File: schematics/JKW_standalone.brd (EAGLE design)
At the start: 159.4 x 80.7 mm, 251 parts, among them IC1 4093D, IC2 LM1458D, IC4 ATMEGA2560-16AU, Q1 BSS84, Q10 BSS84, Q11 BSS84, Q2 BSS84, Q3 BSS84, Q4 BSS84, Q5 BSS84, Q6 BSS84, Q7 BSS84, Q8 BSS84, Q9 BSS84, T1 Mouser: 771-2N7002BK215 , N-C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, T10 Mouser: 771-2N7002BK215 , N-C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, T11 Mouser: 771-2N7002BK215 , N-C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, T12 Mouser: 771-2N7002BK215 , N-C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, T13 Mouser: 771-2N7002BK215 , N-C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, T2 Mouser: 771-2N7002BK215 , N-C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, T3 Mouser: 771-2N7002BK215 , N-C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, T5 Mouser: 771-2N7002BK215 , N-C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, T6 Mouser: 771-2N7002BK215 , N-C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, T7 Mouser: 771-2N7002BK215 , N-C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, T8 Mouser: 771-2N7002BK215 , N-C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, T9 Mouser: 771-2N7002BK215 , N-C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, U4 MCP2515, U5 MCP2551

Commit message: Board equiped with low passes
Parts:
- added C15, C16, C20, C5, C7: 100nF, RCLDT:0805
- R_E2_3, R_E2_4: value n.b. / 0R -> 0R / n.b.
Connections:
- net BL_L_IN: now also C5.1
- net BL_R_IN: now also C7.1
- net GND: now also C15.2, C16.1, C20.1, C5.2, C7.2
- net HB_IN: now also C15.1
- net NG_IN: now also C20.2
- net OIL_PR_IN: now also C16.2
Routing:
- net NG_IN: track 47.9 -> 49.6 mm
- net BL_R_IN: track 19.2 -> 20.4 mm
- net BL_L_IN: track 50.9 -> 52.0 mm
- net OIL_PR_IN: track 66.6 -> 67.3 mm
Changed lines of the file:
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@@
 <?xml version="1.0" encoding="utf-8"?>
 <!DOCTYPE eagle SYSTEM "eagle.dtd">
-<eagle version="6.4">
+<eagle version="6.2">
 <drawing>
 <settings>
@@
 <layer number="27" name="tValues" color="7" fill="1" visible="yes" active="yes"/>
 <layer number="28" name="bValues" color="7" fill="1" visible="yes" active="yes"/>
-<layer number="29" name="tStop" color="7" fill="3" visible="no" active="yes"/>
-<layer number="30" name="bStop" color="7" fill="6" visible="no" active="yes"/>
+<layer number="29" name="tStop" color="7" fill="3" visible="yes" active="yes"/>
+<layer number="30" name="bStop" color="7" fill="6" visible="yes" active="yes"/>
 <layer number="31" name="tCream" color="7" fill="4" visible="yes" active="yes"/>
 <layer number="32" name="bCream" color="7" fill="5" visible="yes" active="yes"/>
@@
 <text x="150" y="20.5" size="1.778" layer="1" font="vector" ratio="20">TOP</text>
 <text x="154.5" y="20.5" size="1.778" layer="16" font="vector" ratio="20" rot="MR0">BOT</text>
-<circle x="5.4" y="16.7" radius="2.5" width="0.4064" layer="39"/>
+<circle x="5.4" y="16.7" radius="3.5" width="0.4064" layer="39"/>
 <circle x="5.9" y="61.8" radius="2.5" width="0.4064" layer="39"/>
 <text x="101.3" y="19.1" size="1.778" layer="16" font="vector" ratio="13" rot="MR0">1</text>
@@
 </class>
 </classes>
-<designrules name="default">
+<designrules>
 <description language="de">DRC von Lutz
 Via´s bis 0.6mm mit Lötstoplack überzogen
@@
 <element name="U4" library="microchip_can" package="SO-18W" value="MCP2515" x="24.3" y="49.9"/>
 <element name="U5" library="skpang_lib" package="SO-08M" value="MCP2551" x="15.5" y="40.2" rot="R180"/>
-<element name="R_E2_3" library="RCLDT" package="0805" value="n.b. / 0R" x="11.7" y="12.4" rot="MR90"/>
-<element name="R_E2_4" library="RCLDT" package="0805" value="n.b. / 0R" x="17.2" y="12.4" rot="MR270"/>
+<element name="R_E2_3" library="RCLDT" package="0805" value="0R / n.b. " x="11.7" y="12.4" rot="MR90"/>
+<element name="R_E2_4" library="RCLDT" package="0805" value="0R / n.b. " x="17.2" y="12.4" rot="MR270"/>
 <element name="R13" library="RCLDT" package="0805" value="4.7k" x="18" y="33.7" rot="R90"/>
 <element name="R10" library="RCLDT" package="0805" value="100" x="10.8" y="37.2"/>
@@
 </element>
 <element name="RX1" library="pinhead" package="1X02" value="" x="61.9" y="8.4" rot="R90"/>
+<element name="C5" library="RCLDT" package="0805" value="100nF" x="11.8" y="21.5"/>
+<element name="C7" library="RCLDT" package="0805" value="100nF" x="34.7" y="34.3" rot="MR0"/>
+<element name="C15" library="RCLDT" package="0805" value="100nF" x="35.3" y="10" rot="MR270"/>
+<element name="C16" library="RCLDT" package="0805" value="100nF" x="41.8" y="14.6" rot="MR270"/>
+<element name="C20" library="RCLDT" package="0805" value="100nF" x="42.4" y="13.4"/>
 </elements>
 <signals>
@@
 <contactref element="U4" pad="9"/>
 <wire x1="22.25" y1="36.1" x2="22" y2="36.1" width="0.254" layer="1"/>
-<via x="33.25" y="35.375" extent="1-16" drill="0.3"/>
+<via x="34.85" y="35.775" extent="1-16" drill="0.3"/>
 <contactref element="R13" pad="1"/>
 <contactref element="C22" pad="1"/>
@@
 <via x="46.25" y="56.15" extent="1-16" drill="0.3"/>
 <via x="34.35" y="48.95" extent="1-16" drill="0.3"/>
+<contactref element="C5" pad="2"/>
+<contactref element="C7" pad="2"/>
+<contactref element="C15" pad="2"/>
+<contactref element="C16" pad="1"/>
+<contactref element="C20" pad="1"/>
 </signal>
 <signal name="DZ">
@@
 <wire x1="42.6" y1="10.8" x2="42.6" y2="12" width="0.254" layer="1"/>
 <via x="42.6" y="12" extent="1-16" drill="0.3"/>
+<contactref element="C20" pad="2"/>
+<wire x1="43.416" y1="13.4" x2="43.416" y2="12.816" width="0.254" layer="1"/>
+<wire x1="43.416" y1="12.816" x2="42.6" y2="12" width="0.254" layer="1"/>
 </signal>
 <signal name="D42">
@@
 <wire x1="8.9" y1="24.9" x2="8.9" y2="22.6" width="0.254" layer="1"/>
 <wire x1="8.9" y1="22.6" x2="7.1" y2="22.6" width="0.254" layer="1"/>
-<wire x1="10.1" y1="19.116" x2="8.9" y2="20.316" width="0.254" layer="1"/>
-<wire x1="8.9" y1="20.316" x2="8.9" y2="22.6" width="0.254" layer="1"/>
+<contactref element="C5" pad="1"/>
+<wire x1="10.1" y1="19.116" x2="10.1" y2="19.932" width="0.254" layer="1"/>
+<wire x1="10.784" y1="20.616" x2="10.784" y2="21.5" width="0.254" layer="1"/>
+<wire x1="10.784" y1="20.616" x2="10.1" y2="19.932" width="0.254" layer="1"/>
+<wire x1="10.784" y1="21.5" x2="10" y2="21.5" width="0.254" layer="1"/>
+<wire x1="10" y1="21.5" x2="8.9" y2="22.6" width="0.254" layer="1"/>
 </signal>
 <signal name="HB_IN">
@@
 <wire x1="23.2" y1="38.316" x2="23.3" y2="38.416" width="0.254" layer="1"/>
 <wire x1="23.3" y1="38.416" x2="26.2" y2="38.416" width="0.254" layer="1"/>
+<contactref element="C15" pad="1"/>
+<wire x1="35.3" y1="11.016" x2="35.316" y2="11.016" width="0.254" layer="16"/>
+<wire x1="35.316" y1="11.016" x2="35.5" y2="11.2" width="0.254" layer="16"/>
 </signal>
 <signal name="BL_R_IN">
@@
 <wire x1="36.94" y1="34.36" x2="36.8" y2="34.5" width="0.254" layer="16"/>
 <via x="36.8" y="34.5" extent="1-16" drill="0.3"/>
-<wire x1="36.8" y1="34.5" x2="28.2" y2="34.5" width="0.254" layer="1"/>
 <via x="26.4" y="34.5" extent="1-16" drill="0.3"/>
+<wire x1="36.8" y1="34.5" x2="28.2" y2="34.5" width="0.254" layer="1"/>
 <wire x1="28.2" y1="34.5" x2="26.4" y2="34.5" width="0.254" layer="1"/>
 <wire x1="28.216" y1="34.484" x2="28.2" y2="34.5" width="0.254" layer="1"/>
@@
 <wire x1="28.3" y1="34.984" x2="28.3" y2="34.6" width="0.254" layer="1"/>
 <wire x1="28.3" y1="34.6" x2="28.2" y2="34.5" width="0.254" layer="1"/>
+<contactref element="C7" pad="1"/>
+<wire x1="35.716" y1="34.3" x2="36.6" y2="34.3" width="0.254" layer="16"/>
+<wire x1="36.6" y1="34.3" x2="36.8" y2="34.5" width="0.254" layer="16"/>
 </signal>
 <signal name="BL_R_IN_H">
@@
 <wire x1="49.8" y1="12.9" x2="50.4" y2="13.5" width="0.254" layer="16"/>
 <contactref element="R_HB1" pad="2"/>
-<wire x1="49.8" y1="12.9" x2="36.1" y2="12.9" width="0.254" layer="16"/>
+<wire x1="49.8" y1="12.9" x2="41.9" y2="12.9" width="0.254" layer="16"/>
+<wire x1="41.9" y1="12.9" x2="36.1" y2="12.9" width="0.254" layer="16"/>
 <wire x1="36.1" y1="12.9" x2="35.4" y2="13.6" width="0.254" layer="16"/>
 <wire x1="35.4" y1="13.6" x2="35.4" y2="31.4" width="0.254" layer="16"/>
@@
 <via x="21.5" y="33.2" extent="1-16" drill="0.3"/>
 <wire x1="21.5" y1="33.2" x2="21.5" y2="32.016" width="0.254" layer="16"/>
+<contactref element="C16" pad="2"/>
+<wire x1="41.8" y1="13.584" x2="41.8" y2="13" width="0.254" layer="16"/>
+<wire x1="41.8" y1="13" x2="41.9" y2="12.9" width="0.254" layer="16"/>
 </signal>
 <signal name="N$2">

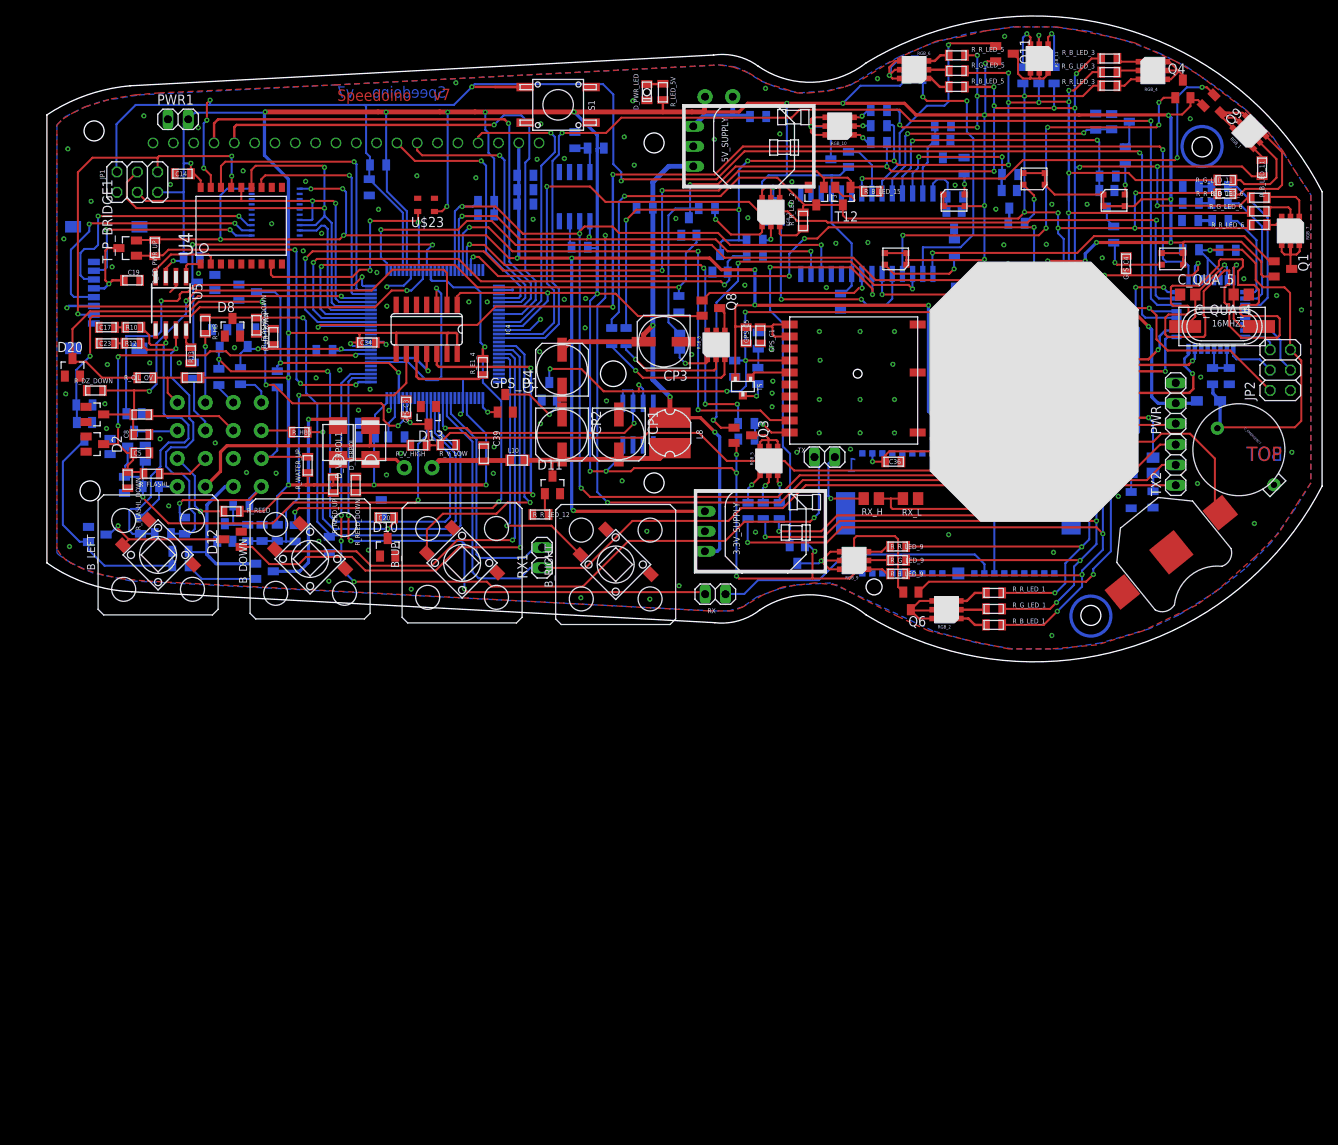
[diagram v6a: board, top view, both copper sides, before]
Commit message: Added TMC222
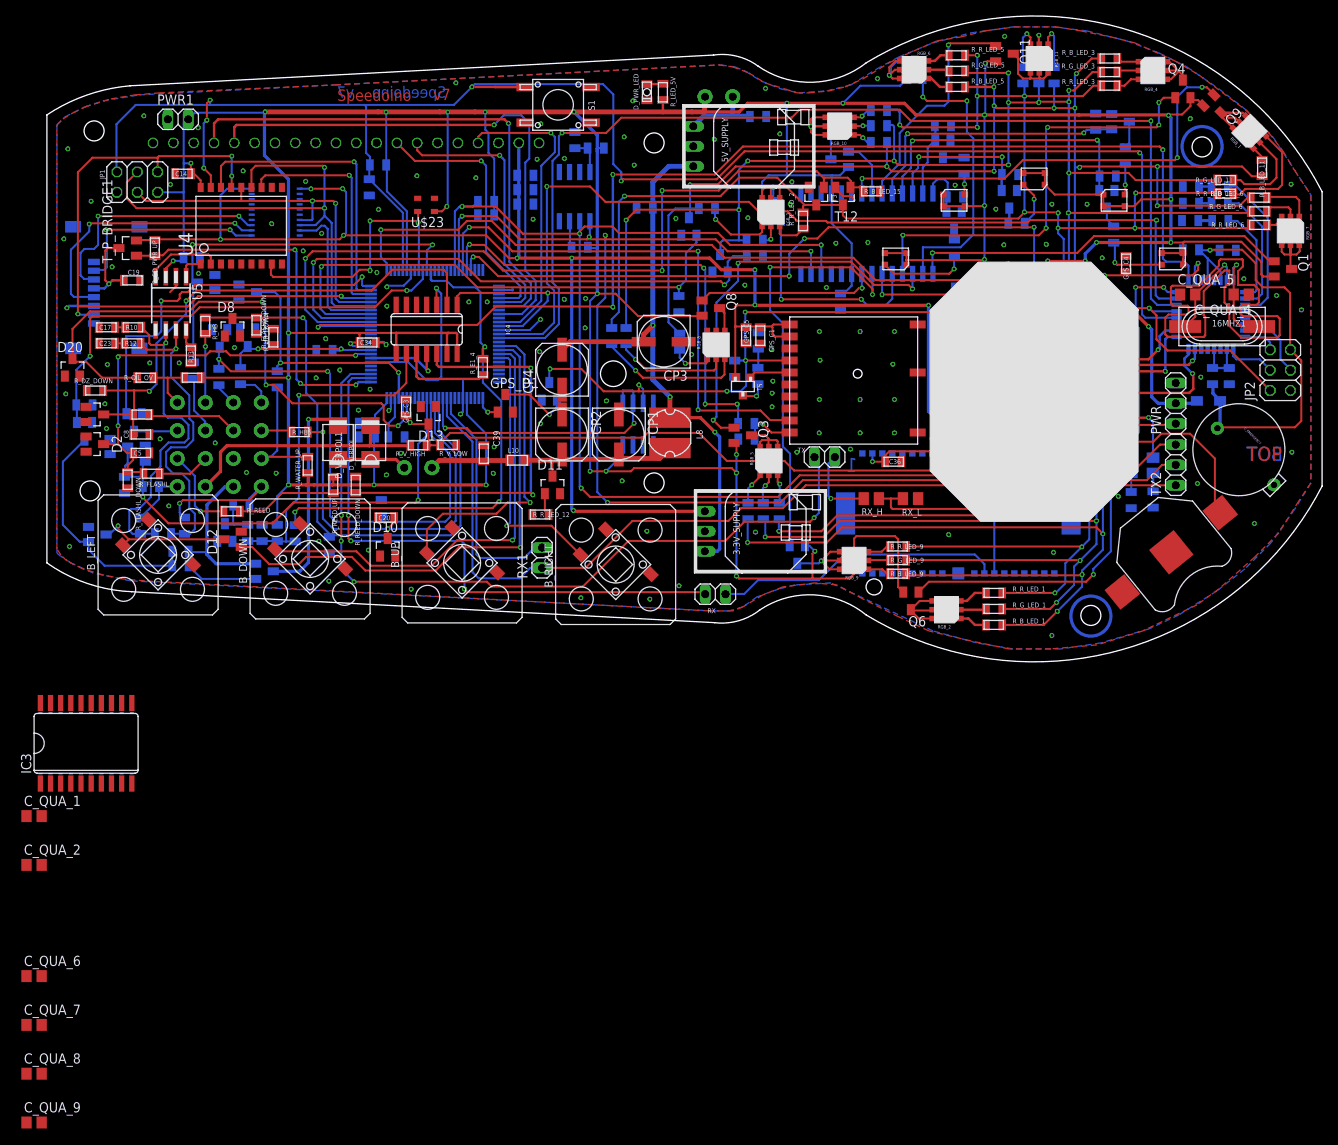
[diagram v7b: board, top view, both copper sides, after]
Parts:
- added C_QUA_1: Tantal 1µF, rcl:C0805
- added C_QUA_2, C_QUA_8: 100nF, rcl:C0805
- added C_QUA_6, C_QUA_7: 220nF, rcl:C0805
- added C_QUA_9: Tantal 100µF, rcl:C0805
- added IC3: TMC222, tmc:SOIC20
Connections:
- new net N$114: IC3.15, STEPPER.1-
- new net N$116: C_QUA_6.2, IC3.10
- new net N$117: C_QUA_6.1, IC3.9
- new net N$118: C_QUA_7.2, IC3.11
- new net N$35: IC3.18, STEPPER.2-
- new net N$36: IC3.16, STEPPER.2+
- new net N$48: IC3.13, STEPPER.1+
- net BAT+: now also C_QUA_7.1, C_QUA_8.1, C_QUA_9.1, IC3.12, IC3.19
- net GND: now also C_QUA_1.1, C_QUA_2.2, C_QUA_8.2, C_QUA_9.2, IC3.14, IC3.17, IC3.20, IC3.4, IC3.5, IC3.7, IC3.8
- net M1: no longer STEPPER.1+
- net M2: no longer STEPPER.1-
- net M3: no longer STEPPER.2+
- net M4: no longer STEPPER.2-
- net SCL: now also IC3.2
- net SDA: now also IC3.1
- net VDD: now also C_QUA_1.2, C_QUA_2.1, IC3.3
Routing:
- net M3: track 33.6 -> 16.8 mm
- net M4: track 28.4 -> 17.1 mm
- net M1: track 15.5 -> 12.4 mm
- net M2: track 16.6 -> 14.5 mm

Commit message: Removed TMC222
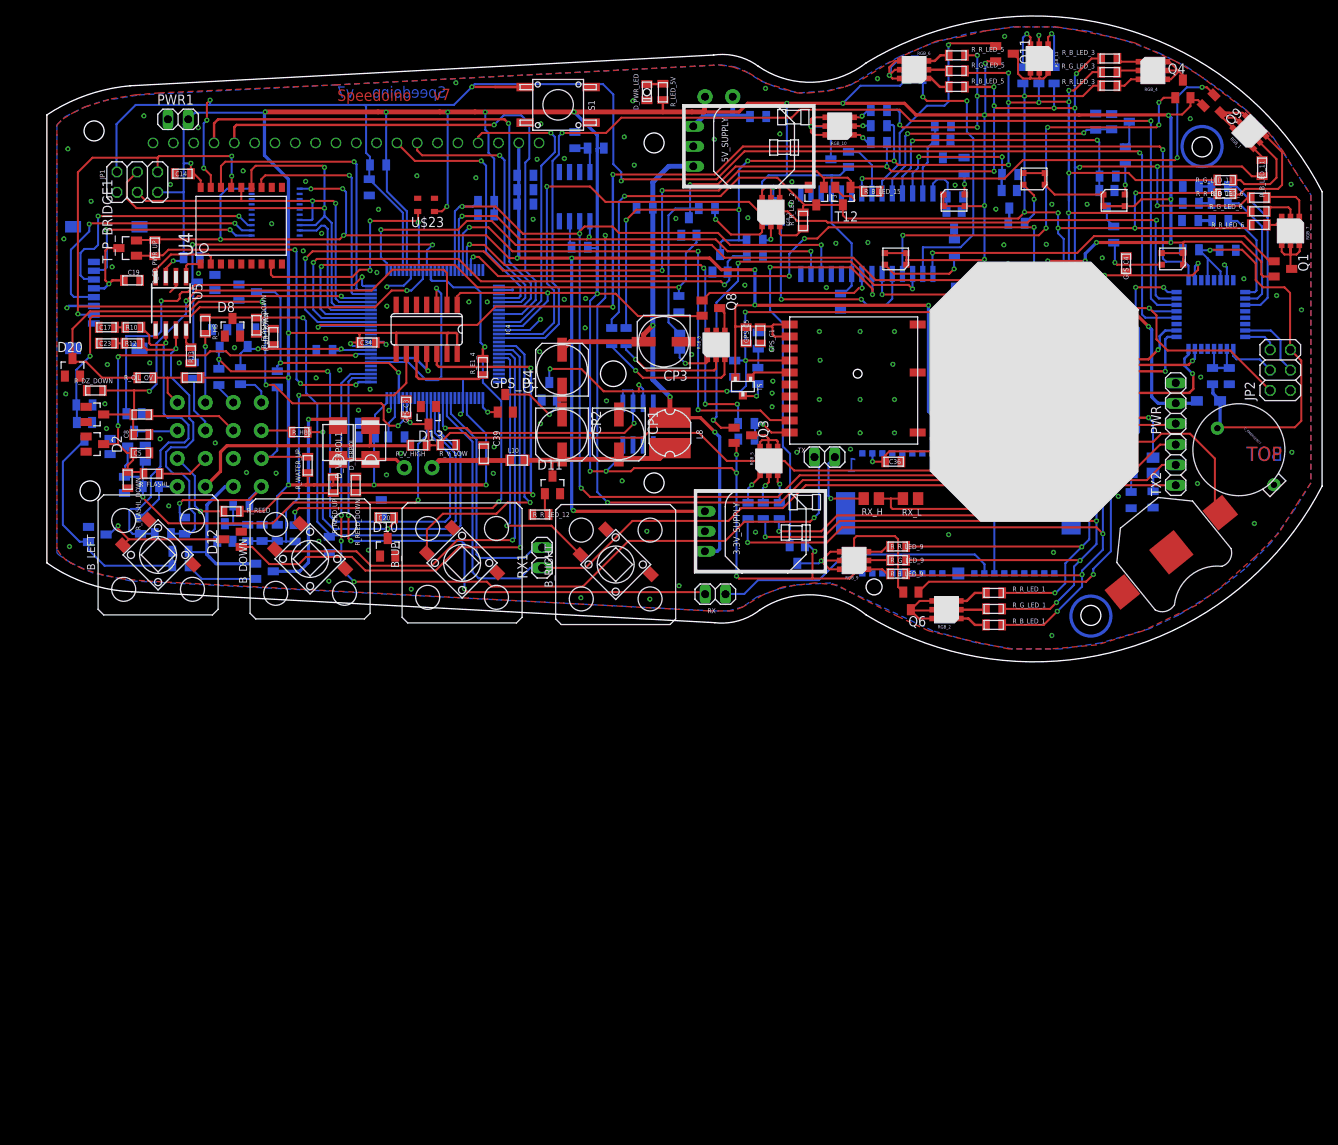
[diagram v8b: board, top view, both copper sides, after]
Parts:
- removed 16MHZ1: 16Mhz, XT:XT-HC49S-SMD
- removed C_QUA_1: Tantal 1µF, rcl:C0805
- removed C_QUA_2, C_QUA_8: 100nF, rcl:C0805
- removed C_QUA_4, C_QUA_5: 22pF, rcl:C0805
- removed C_QUA_6, C_QUA_7: 220nF, rcl:C0805
- removed C_QUA_9: Tantal 100µF, rcl:C0805
- removed IC3: TMC222, tmc:SOIC20
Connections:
- removed net N$114: IC3.15, STEPPER.1-
- removed net N$116: C_QUA_6.2, IC3.10
- removed net N$117: C_QUA_6.1, IC3.9
- removed net N$118: C_QUA_7.2, IC3.11
- removed net N$35: IC3.18, STEPPER.2-
- removed net N$36: IC3.16, STEPPER.2+
- removed net N$48: IC3.13, STEPPER.1+
- removed net N$63: 16MHZ1.1, C_QUA_5.2, U$1.7
- removed net N$65: 16MHZ1.2, C_QUA_4.2, U$1.8
- net 16MHZ: now also U$1.7
- net BAT+: no longer C_QUA_7.1, C_QUA_8.1, C_QUA_9.1, IC3.12, IC3.19
- net GND: no longer C_QUA_1.1, C_QUA_2.2, C_QUA_4.1, C_QUA_5.1, C_QUA_8.2, C_QUA_9.2, IC3.14, IC3.17, IC3.20, IC3.4, IC3.5, IC3.7, IC3.8
- net M1: now also STEPPER.1+
- net M2: now also STEPPER.1-
- net M3: now also STEPPER.2+
- net M4: now also STEPPER.2-
- net SCL: no longer IC3.2
- net SDA: no longer IC3.1
- net VDD: no longer C_QUA_1.2, C_QUA_2.1, IC3.3
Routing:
- net GND: track 100.8 -> 31.2 mm
- net M3: track 16.8 -> 33.6 mm
- net N$65: track 12.5 -> 0.00 mm, vias 1 -> 0
- net N$63: track 11.8 -> 0.00 mm, vias 1 -> 0
- net M4: track 17.1 -> 28.4 mm
- net M1: track 12.4 -> 15.5 mm
- net M2: track 14.5 -> 16.6 mm
- net 16MHZ: track 34.0 -> 36.1 mm, vias 3 -> 4
